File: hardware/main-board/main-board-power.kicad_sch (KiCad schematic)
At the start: 32 parts, among them J1 Power Board, J8 DMX512, U1 RT8258, U2 RT8258

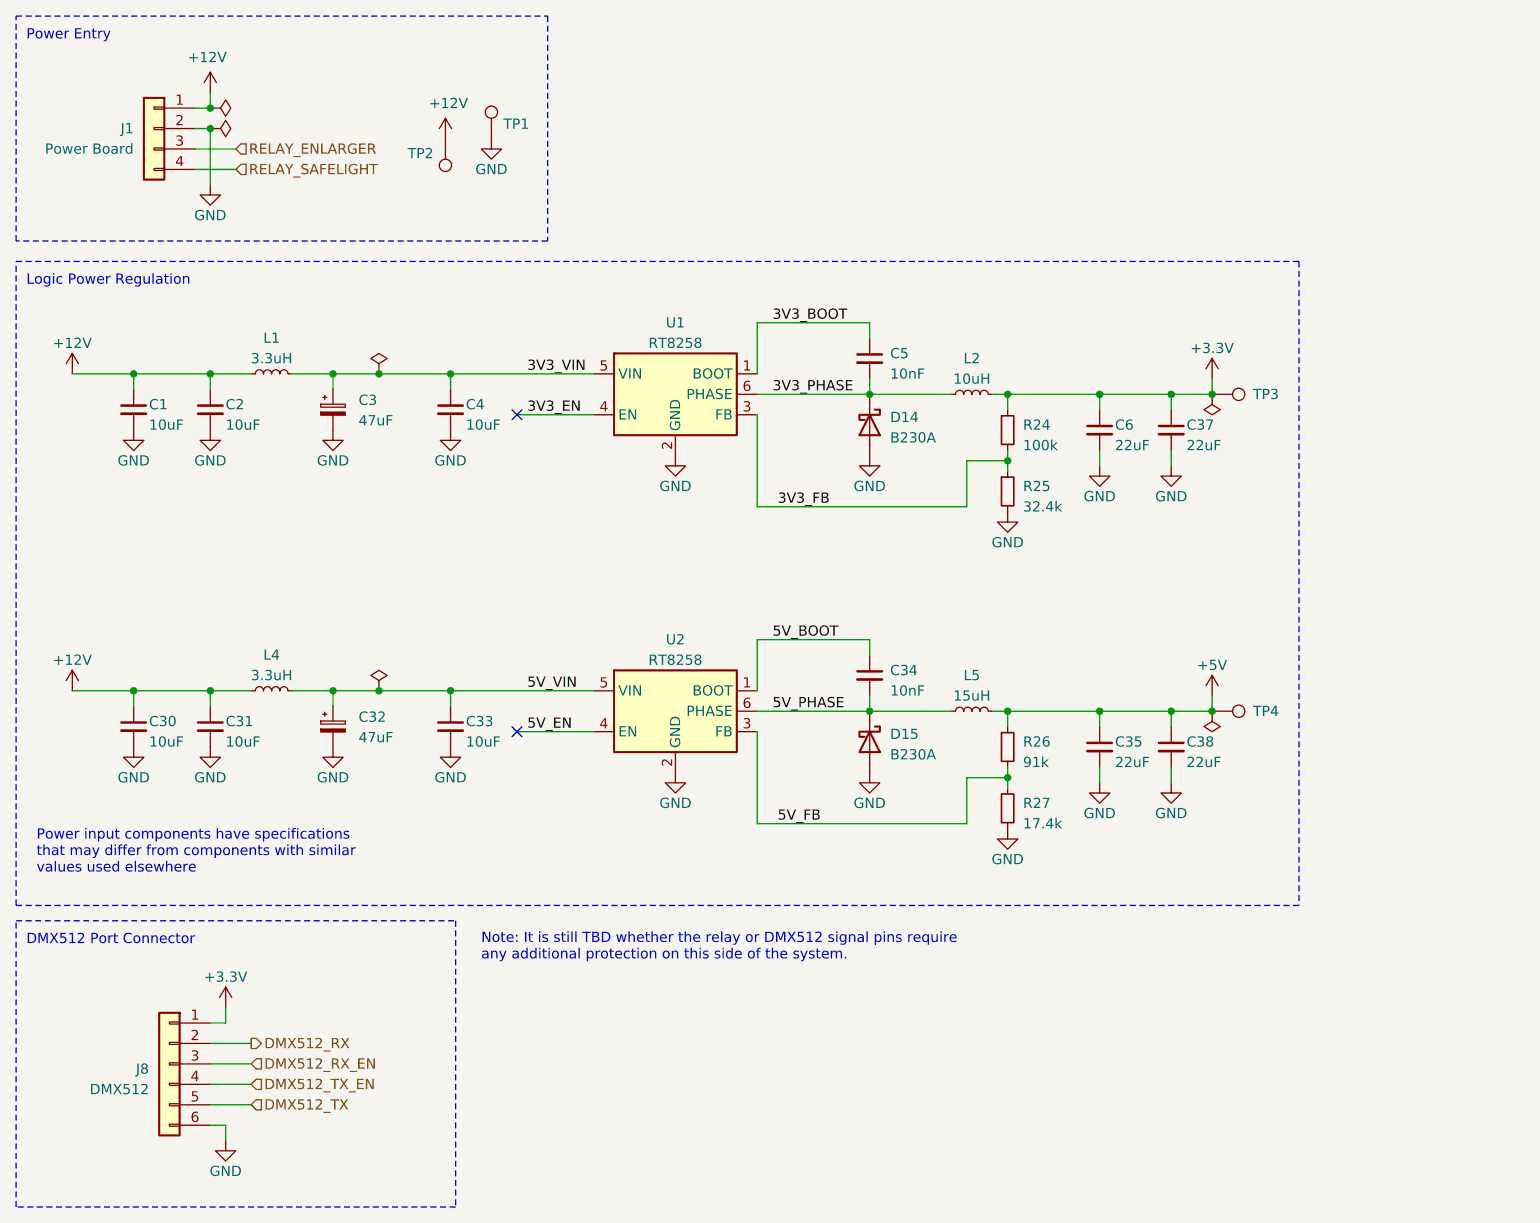
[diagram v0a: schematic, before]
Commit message: Schematic updates for power regulator filtering and meter interface
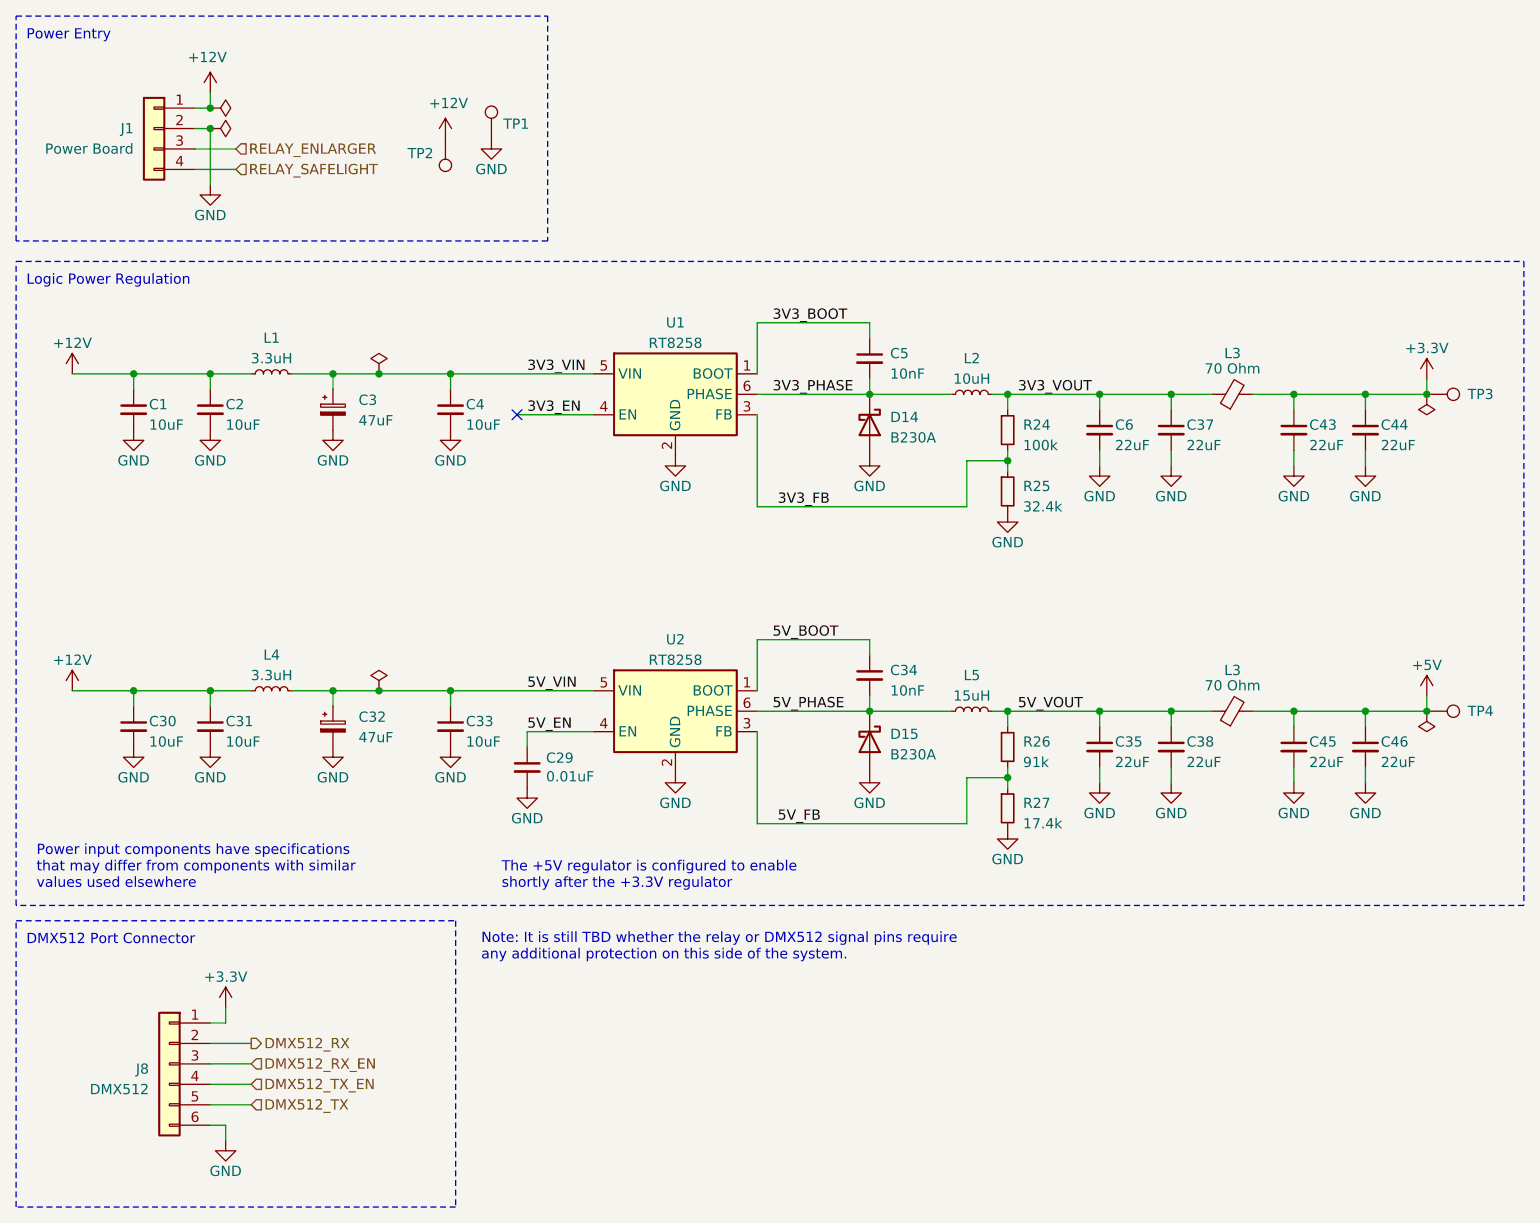
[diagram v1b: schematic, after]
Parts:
- added C29: 0.01uF, Capacitor_SMD:C_0603_1608Metric, symbol Device:C_Small
- added C43, C44, C45, C46: 22uF, Capacitor_SMD:C_1206_3216Metric, symbol Device:C_Small
- added L3 (x2): 70 Ohm, Inductor_SMD:L_0603_1608Metric, symbol Device:FerriteBead_Small
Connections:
- net +3.3V: now also C43.1, C44.1, L3.2; no longer C37.1, C6.1, L2.2, R24.1
- net +5V: now also C45.1, C46.1, L3.2; no longer C35.1, C38.1, L5.2, R26.1
- net 5V_EN: now also C29.1
- net GND: now also C29.2, C43.2, C44.2, C45.2, C46.2
- new net 3V3_VOUT: C37.1, C6.1, L2.2, L3.1, R24.1
- new net 5V_VOUT: C35.1, C38.1, L3.1, L5.2, R26.1
- no-connect marks 2 -> 1
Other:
- note added: "The +5V regulator is configured to enable shortly after the +3.3V regulator"
- moved on the sheet: TP3, TP4

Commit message: Renumbered reference designators on main board
This board has changed so much that its better to take this hit than
have the numbers appear random during board assembly.
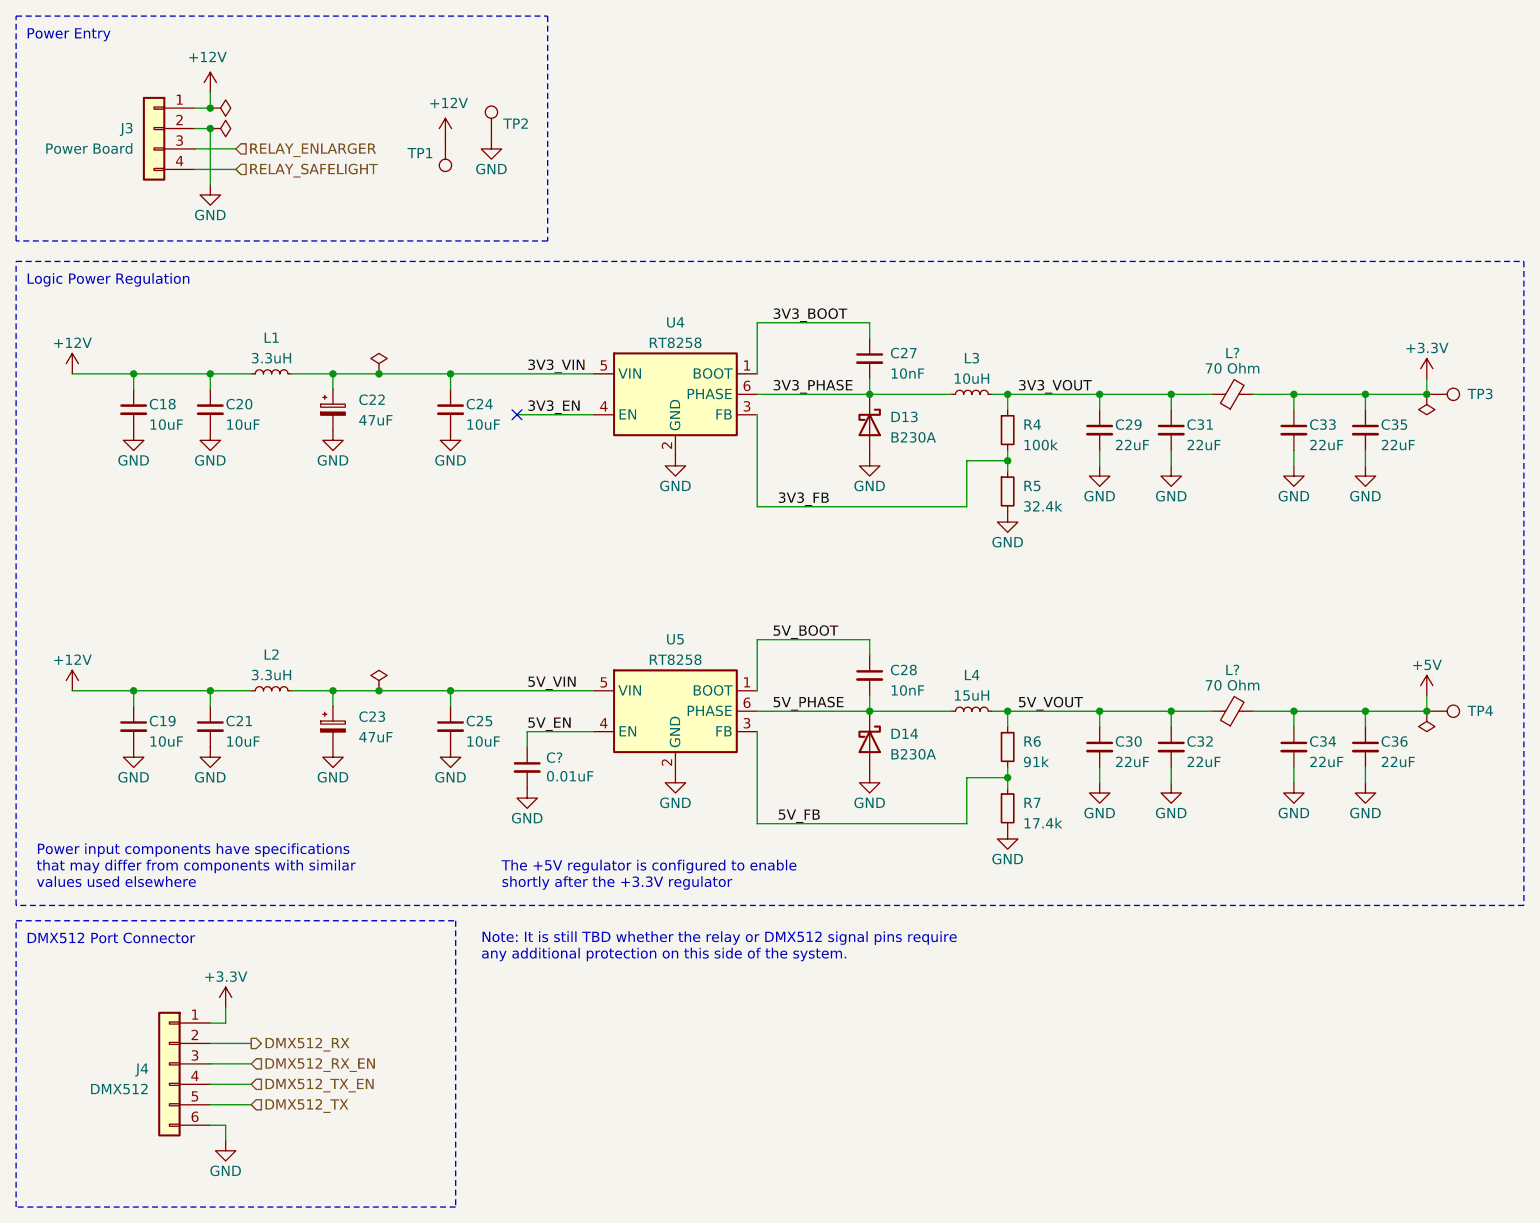
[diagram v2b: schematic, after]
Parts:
- renumbered C1 to C18, C30 to C19, C2 to C20, C31 to C21, C3 to C22, C32 to C23, C4 to C24, C33 to C25, C5 to C27, C34 to C28, C6 to C29, C35 to C30, C37 to C31, C38 to C32, C43 to C33, C45 to C34, C44 to C35, C46 to C36, C29 to C?, D14 to D13, D15 to D14, J1 to J3, J8 to J4, L4 to L2, L2 to L3, L5 to L4, L3 to L?, R24 to R4, R25 to R5, R26 to R6, R27 to R7, TP2 to TP1, TP1 to TP2, U1 to U4, U2 to U5

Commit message: Various BOM tweaks
Merged all 0.01uF 0603 capacitors to use the same 50V rated part, to
avoid needing separate components for power and non-power use cases.

Switched panel LED current resistor tolerance from 5% to 1% for better
unit-to-unit consistency.
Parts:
- C27, C28: value 10nF -> 0.01uF
- C?: Manufacturer PN CL10B103KA8NNNC -> CL10B103KB8NNNC; Supplier PN 1276-1132-1-ND -> 1276-1009-1-ND
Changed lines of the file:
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@@
       (effects (font (size 1.27 1.27)) (justify left))
     )
-    (property "Value" "10nF" (at 124.46 99.7013 0)
+    (property "Value" "0.01uF" (at 124.46 99.7013 0)
       (effects (font (size 1.27 1.27)) (justify left))
     )
@@
       (effects (font (size 1.27 1.27)) (justify left))
     )
-    (property "Value" "10nF" (at 124.46 60.3313 0)
+    (property "Value" "0.01uF" (at 124.46 60.3313 0)
       (effects (font (size 1.27 1.27)) (justify left))
     )
@@
       (effects (font (size 1.27 1.27)) hide)
     )
-    (property "Datasheet" "https://media.digikey.com/pdf/Data%20Sheets/Samsung%20PDFs/CL_Series_MLCC_ds.pdf" (at 79.375 109.22 0)
-      (effects (font (size 1.27 1.27)) hide)
-    )
-    (property "Description" "CAP CER 10000PF 25V X7R 0603" (at 79.375 109.22 0)
+    (property "Datasheet" "https://media.digikey.com/pdf/Data%20Sheets/Samsung%20PDFs/CL10B103KB8NNNC_Spec.pdf" (at 79.375 109.22 0)
+      (effects (font (size 1.27 1.27)) hide)
+    )
+    (property "Description" "CAP CER 10000PF 50V X7R 0603" (at 79.375 109.22 0)
       (effects (font (size 1.27 1.27)) hide)
     )
@@
       (effects (font (size 1.27 1.27)) hide)
     )
-    (property "Manufacturer PN" "CL10B103KA8NNNC" (at 79.375 109.22 0)
+    (property "Manufacturer PN" "CL10B103KB8NNNC" (at 79.375 109.22 0)
       (effects (font (size 1.27 1.27)) hide)
     )
@@
       (effects (font (size 1.27 1.27)) hide)
     )
-    (property "Supplier PN" "1276-1132-1-ND" (at 79.375 109.22 0)
-      (effects (font (size 1.27 1.27)) hide)
-    )
+    (property "Supplier PN" "1276-1009-1-ND" (at 79.375 109.22 0)
+      (effects (font (size 1.27 1.27)) hide)
+    )
